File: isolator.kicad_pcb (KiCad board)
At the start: 4 copper layers, 120 x 75 mm, 125 parts, among them J1 HOST, J2 USB_C_Receptacle_PowerOnly_6P, J3 USB_A, J4 USB_A, J5 USB_C_Receptacle_USB2.0_16P, J6 USB_C_Receptacle_USB2.0_16P, Q1 2N7002, Q2 2N7002, T1 750313638, U1 ADuM4165, U10 TPS2553DBV, U11 TPS2553DBV, U12 TPS2553DBV, U13 TLV7041DBV, U14 TLV7041DBV, U15 USBLC6-2SC6, U16 USBLC6-2SC6, U17 USBLC6-2SC6, U18 USBLC6-2SC6, U2 USBLC6-2SC6, U3 USBLC6-2SC6, U4 USB2514B_Bi, U5 SN6505BDBV, U6 MIC29302WU, U7 TPS2121, U8 AP2112K-3.3, U9 TPS2553DBV, Y1 24M 8pF, Y2 24M 12pF

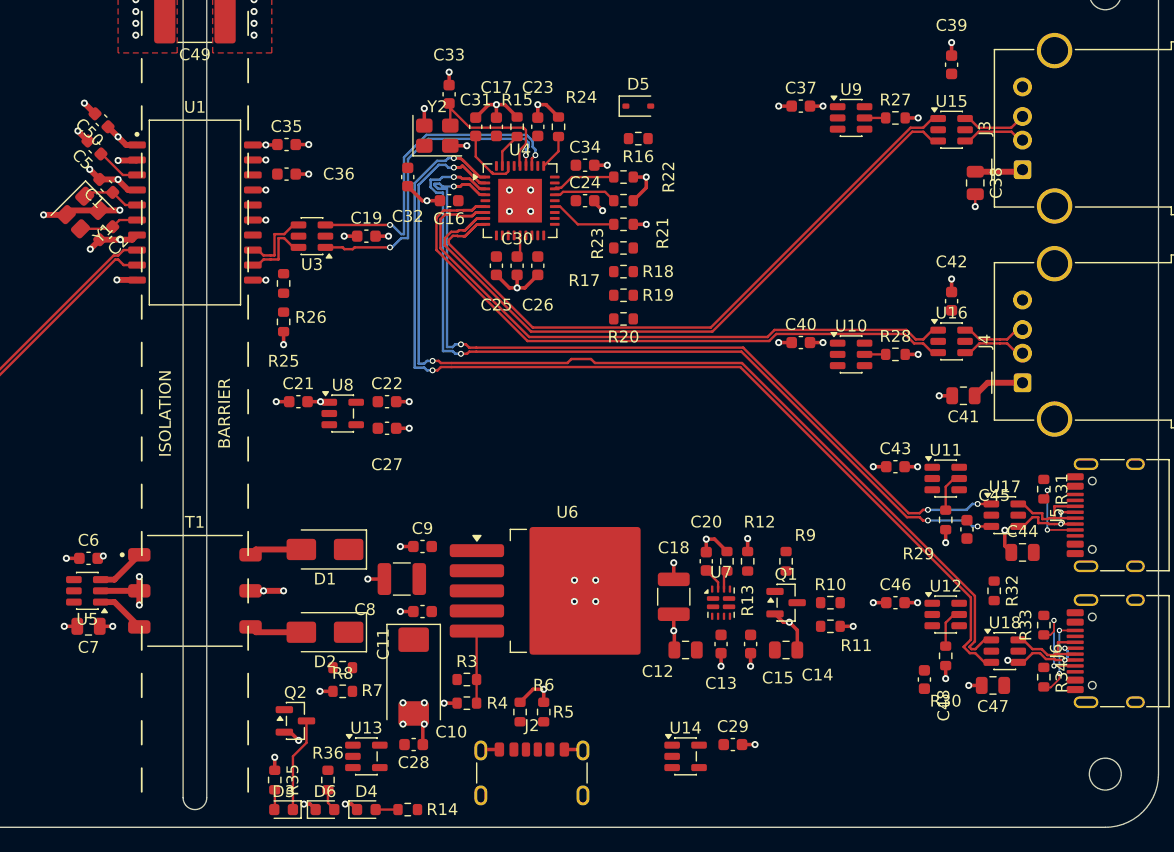
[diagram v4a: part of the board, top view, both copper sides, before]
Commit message: feat(pcb): autoroute remaining nets via Freerouting pipeline — 110 nets landed (146->36 unconnected), pairs verified conserved, planes locked out, PGOOD2 barrier fix
Co-Authored-By: Claude Fable 5 <noreply@anthropic.com>
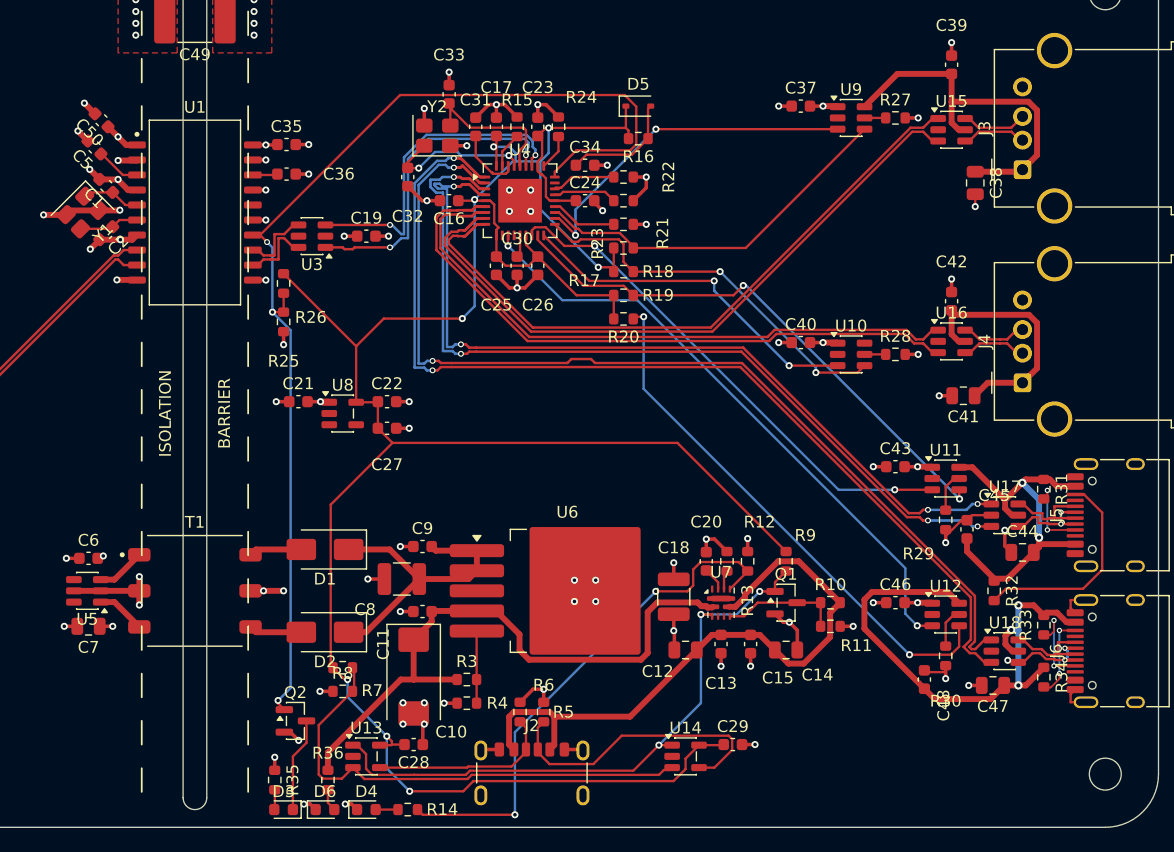
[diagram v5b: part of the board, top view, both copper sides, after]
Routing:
- net /ISO_3V3: track 0.00 -> 215.9 mm, vias 0 -> 8
- net /PGOOD2: track 0.00 -> 93.6 mm, vias 0 -> 3
- net /EXT_5V: track 0.00 -> 54.0 mm
- net /n3A_DET: track 0.00 -> 52.5 mm, vias 0 -> 3
- net /PRTPWR4: track 0.00 -> 52.3 mm, vias 0 -> 2
- net /DCDC_5V: track 0.00 -> 51.9 mm
- net /nOCS3: track 0.00 -> 46.6 mm, vias 0 -> 2
- net /P4_VBUS: track 0.00 -> 45.6 mm, vias 0 -> 3
- net /nOCS4: track 0.00 -> 45.1 mm, vias 0 -> 2
- net /ST_IND: track 0.00 -> 44.3 mm, vias 0 -> 2
- net /PRTPWR3: track 0.00 -> 43.6 mm, vias 0 -> 2
- net /VTH: track 0.00 -> 41.6 mm
- net /nOCS2: track 0.00 -> 32.9 mm, vias 0 -> 2
- net /P3_VBUS: track 0.00 -> 32.5 mm, vias 0 -> 2
- net /nOCS1: track 0.00 -> 31.7 mm
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
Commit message: wip(4port): save in-progress 4-port schematic/PCB edits before archiving
Snapshot of the uncommitted work on the 4-port isolator so it is preserved
before the repo collapses to the single-port design at the root.

State of this snapshot: ERC reports 3 errors, all U7 (TPS2121) pin 4 OV2
disconnected. That is pre-existing, in-progress work on the 4-port design --
it is NOT a regression introduced here and is deliberately left unfixed.

This commit is the tip of branch 4port-archive; main proceeds without the
4-port project.

Co-Authored-By: Claude Opus 5 <noreply@anthropic.com>
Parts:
- moved R25 2.46 mm to (97.4, 82.3)
- moved R26 2.46 mm to (97.4, 79.0)
- moved U3 1.92 mm to (99.1, 74.8)
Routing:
- net /nOCS4: track 45.1 -> 61.5 mm, vias 2 -> 4
- net /ISO_D+: track 33.4 -> 26.7 mm
- net /ISO_D-: track 33.9 -> 27.3 mm
- net /HUB_RESET: track 9.88 -> 12.4 mm
- net /PGOOD2: track 93.6 -> 95.9 mm
- net /ISO_3V3: track 215.9 -> 213.7 mm

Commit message: refactor: collapse repo to the single-port isolator at the root
The single-port design is the one that ships, so it moves up from v1/ and
becomes the only KiCad project in the repo. The 4-port design is archived on
branch 4port-archive (tip ef23a53) and removed from main.

Moved (via git mv, history preserved):
  v1/isolator-v1.kicad_{sch,pcb,pro,dru} -> isolator.kicad_{sch,pcb,pro,dru}
  v1/isolator-v1-bom.csv                 -> isolator-bom.csv
  v1/{sym,fp}-lib-table                  -> {sym,fp}-lib-table
  analysis-v1/                           -> analysis/

Deleted (4-port project and its artifacts): isolator.kicad_{sch,pcb,pro,prl,dru},
isolator-erc.rpt, isolator-backups/, analysis/, logs/. Kept isolator-lib.kicad_sym,
isolator-lib.pretty/, datasheets/, docs/, tools/.

Path and self-reference fixes the move required:
  - {sym,fp}-lib-table URIs: ${KIPRJMOD}/../isolator-lib.* -> ${KIPRJMOD}/isolator-lib.*
  - isolator.kicad_pro: meta.filename and schematic.top_level_sheets[0].filename/name,
    plus sheets[0]. The sheet UUID already matched the schematic root uuid
    (00000000-0000-0000-0000-000000000001) and was left alone. kicad-cli never
    reads these fields, so nothing but a GUI open would have caught them.
  - isolator.kicad_sch: 62 (project "isolator-v1") instance blocks -> "isolator",
    so the GUI keeps its per-project symbol instance data.
  - Schematic text block "V1 LAYOUT CONSTRAINTS -- BINDING" -> "LAYOUT CONSTRAINTS
    -- BINDING"; title block "Isolated USB 2.0 Cable — v1" -> "Isolated USB 2.0
    Cable". Rev "v1.0" left as-is: that is a revision, not a design name.
  - docs/superpowers/{specs,plans,reviews}/*.md: paths updated, "v1" as a design
    name rewritten to "the isolator", "v2" to "the archived 4-port design".
    References to the 4-port files now read 4port-archive:isolator.kicad_sch, since
    that path at the root means the single-port design now. Every doc carries a
    dated banner explaining the restructure; past-tense decisi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
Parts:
- removed C1, C2: 8p, Capacitor_SMD:C_0603_1608Metric
- removed C10: 47u, Capacitor_Tantalum_SMD:CP_EIA-7343-31_Kemet-D
- removed C11, C13, C15, C16, C17, C19, C20, C23, C24, C25, C26, C27, C28, C29, C30, C31, C35, C36, C37, C39, C40, C42, C43, C45, C46, C48, C6, C9: 0.1u, Capacitor_SMD:C_0603_1608Metric
- removed C12, C14, C3, C7: 10u, Capacitor_SMD:C_0805_2012Metric
- removed C18, C8: 47u, Capacitor_SMD:C_1210_3225Metric
- removed C21, C22, C34: 1u, Capacitor_SMD:C_0603_1608Metric
- removed C32, C33: 18p, Capacitor_SMD:C_0603_1608Metric
- removed C38, C41, C44, C47: 22u, Capacitor_SMD:C_0805_2012Metric
- removed C4, C5, C50: 100n, Capacitor_SMD:C_0603_1608Metric
- removed C49: 1nF 2kV DNP, Capacitor_SMD:C_2220_5750Metric
- removed D1, D2: SS34, Diode_SMD:D_SMA
- removed D3, D4, D6: LED, LED_SMD:LED_0603_1608Metric
- removed D5: 1N4148WS, Diode_SMD:D_SOD-323
- removed J1: HOST, Connector_USB:USB_C_Receptacle_HRO_TYPE-C-31-M-12
- removed J2: USB_C_Receptacle_PowerOnly_6P, Connector_USB:USB_C_Receptacle_GCT_USB4125-xx-x_6P_TopMnt_Horizontal
- removed J3, J4: USB_A, Connector_USB:USB_A_Molex_67643_Horizontal
- removed J5, J6: USB_C_Receptacle_USB2.0_16P, Connector_USB:USB_C_Receptacle_HRO_TYPE-C-31-M-12
- removed MH1, MH2, MH3, MH4: MountingHole_2.7mm_M2.5_DIN965, MountingHole:MountingHole_2.7mm_M2.5_DIN965
- removed Q1, Q2: 2N7002, Package_TO_SOT_SMD:SOT-23
- removed R1, R2, R5, R6: 5.1k, Resistor_SMD:R_0603_1608Metric
- removed R10, R17, R18, R19, R20, R25, R26, R9: 100k, Resistor_SMD:R_0603_1608Metric
- removed R11, R23, R24: 47k, Resistor_SMD:R_0603_1608Metric
- removed R12: 35.7k, Resistor_SMD:R_0603_1608Metric
- removed R13, R16, R21, R22, R4, R8: 10k, Resistor_SMD:R_0603_1608Metric
- removed R14, R35: 1k, Resistor_SMD:R_0603_1608Metric
- removed R15: 12.0k, Resistor_SMD:R_0603_1608Metric
- removed R27, R28, R29, R30: 40.2k, Resistor_SMD:R_0603_1608Metric
- removed R3: 30.1k, Resistor_SMD:R_0603_1608Metric
- removed R31, R32, R33, R34: 56k, Resistor_SMD:R_0603_1608Metric
- removed R36: 330R, Resistor_SMD:R_0603_1608Metric
- removed R7: 16.9k, Resistor_SMD:R_0603_1608Metric
- removed T1: 750313638, isolator-lib:WE_750313638
- removed U1: ADuM4165, isolator-lib:ADI_SOIC_IC_20_RI-20-1
- removed U10, U11, U12, U9: TPS2553DBV, Package_TO_SOT_SMD:SOT-23-6
- removed U13, U14: TLV7041DBV, Package_TO_SOT_SMD:SOT-23-5
- removed U15, U16, U17, U18, U2, U3: USBLC6-2SC6, Package_TO_SOT_SMD:SOT-23-6
- removed U4: USB2514B_Bi, Package_DFN_QFN:QFN-36-1EP_6x6mm_P0.5mm_EP3.7x3.7mm
- removed U5: SN6505BDBV, Package_TO_SOT_SMD:SOT-23-6
- removed U6: MIC29302WU, Package_TO_SOT_SMD:TO-263-5_TabPin3
- removed U7: TPS2121, Package_DFN_QFN:Texas_VQFN-HR-12_2x2.5mm_P0.5mm
- removed U8: AP2112K-3.3, Package_TO_SOT_SMD:SOT-23-5
- removed Y1: 24M 8pF, Crystal:Crystal_SMD_3225-4Pin_3.2x2.5mm
- removed Y2: 24M 12pF, Crystal:Crystal_SMD_3225-4Pin_3.2x2.5mm
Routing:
- net /ISO_3V3: track 213.7 -> 0.00 mm, vias 8 -> 0
- net GND2: track 109.1 -> 0.00 mm, vias 71 -> 0
- net /P4_D-: track 96.5 -> 0.00 mm, vias 5 -> 0
- net /PGOOD2: track 95.9 -> 0.00 mm, vias 3 -> 0
- net /P4_D+: track 95.8 -> 0.00 mm, vias 2 -> 0
- net /P3_D-: track 84.0 -> 0.00 mm, vias 6 -> 0
- net /P3_D+: track 83.4 -> 0.00 mm, vias 4 -> 0
- net /P1_D-: track 64.6 -> 0.00 mm
- net /P1_D+: track 63.5 -> 0.00 mm
- net /nOCS4: track 61.5 -> 0.00 mm, vias 4 -> 0
- net /P2_D-: track 61.3 -> 0.00 mm
- net /P2_D+: track 60.2 -> 0.00 mm
- net /EXT_5V: track 54.0 -> 0.00 mm
- net /n3A_DET: track 52.5 -> 0.00 mm, vias 3 -> 0
- net /PRTPWR4: track 52.3 -> 0.00 mm, vias 2 -> 0
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- removed copper zone on In2.Cu, net /ISO_5V
- removed copper zone on In2.Cu, net /VBUS_HOST
- removed copper zone on F.Cu, net GND1
- removed copper zone on In1.Cu, net GND1
- removed copper zone on F.Cu, net GND2
- removed copper zone on In1.Cu, net GND2
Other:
- board outline removed
- board text removed: "BARRIER"
- board text removed: "ISOLATION"

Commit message: feat(pcb): board skeleton -- 120x50 outline, JLC04161H-7628 stackup, edge keepouts, Gate 2
Also corrects the stackup's source branch in the spec and plan. It is on
claude/jlcpcb-design-rules-4layer-6d6ae1 (5c56d3e), not 4port-archive -- the
archived 4-port board still carries the stale 2-layer stackup (1.51mm core,
Er 4.5) that 5c56d3e was written to replace.

The plan's sed-based extraction was also wrong: a sed range on
/(stackup/,/^\t\t)/ closes early on this file and drops In1.Cu and In2.Cu while
still yielding balanced parentheses, so the truncation reads as success. Now
extracted by paren matching.

Co-Authored-By: Claude Opus 5 <noreply@anthropic.com>
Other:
- board outline added: 120 x 50 mm
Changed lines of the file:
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@@
 	(layers
 		(0 "F.Cu" signal)
-		(4 "In1.Cu" signal "GND")
-		(6 "In2.Cu" signal "PWR")
+		(4 "In1.Cu" signal "GND_SPLIT_A")
+		(6 "In2.Cu" signal "GND_SPLIT_B")
 		(2 "B.Cu" signal)
 		(9 "F.Adhes" user "F.Adhesive")
@@
 		(33 "B.Fab" user)
 	)
+	(setup
+		(stackup
+			(layer "F.SilkS"
+				(type "Top Silk Screen")
+			)
+			(layer "F.Paste"
+				(type "Top Solder Paste")
+			)
+			(layer "F.Mask"
+				(type "Top Solder Mask")
+				(color "Green")
+				(thickness 0.01)
+			)
+			(layer "F.Cu"
+				(type "copper")
+				(thickness 0.035)
+			)
+			(layer "dielectric 1"
+				(type "prepreg")
+				(thickness 0.2104)
+				(material "FR4")
+				(epsilon_r 4.4)
+				(loss_tangent 0.02)
+			)
+			(layer "In1.Cu"
+				(type "copper")
+				(thickness 0.0152)
+			)
+			(layer "dielectric 2"
+				(type "core")
+				(thickness 1.065)
+				(material "FR4")
+				(epsilon_r 4.6)
+				(loss_tangent 0.02)
+			)
+			(layer "In2.Cu"
+				(type "copper")
+				(thickness 0.0152)
+			)
+			(layer "dielectric 3"
+				(type "prepreg")
+				(thickness 0.2104)
+				(material "FR4")
+				(epsilon_r 4.4)
+				(loss_tangent 0.02)
+			)
+			(layer "B.Cu"
+				(type "copper")
+				(thickness 0.035)
+			)
+			(layer "B.Mask"
+				(type "Bottom Solder Mask")
+				(color "Green")
+				(thickness 0.01)
+			)
+			(layer "B.Paste"
+				(type "Bottom Solder Paste")
+			)
+			(layer "B.SilkS"
+				(type "Bottom Silk Screen")
+			)
+			(copper_finish "None")
+			(dielectric_constraints no)
+		)
+		(pad_to_mask_clearance 0)
+		(allow_soldermask_bridges_in_footprints no)
+		(tenting
+			(front yes)
+			(back yes)
+		)
+		(covering
+			(front no)
+			(back no)
+		)
+		(plugging
+			(front no)
+			(back no)
+		)
+		(capping no)
+		(filling no)
+		(pcbplotparams
+			(layerselection 0x00000000_00000000_55555555_5755f5ff)
+			(plot_on_all_layers_selection 0x00000000_00000000_00000000_00000000)
+			(disableapertmacros no)
+			(usegerberextensions no)
+			(usegerberattributes yes)
+			(usegerberadvancedattributes yes)
+			(creategerberjobfile yes)
+			(dashed_line_dash_ratio 12)
+			(dashed_line_gap_ratio 3)
+			(svgprecision 4)
+			(plotframeref no)
+			(mode 1)
+			(useauxorigin no)
+			(pdf_front_fp_property_popups yes)
+			(pdf_back_fp_property_popups yes)
+			(pdf_metadata yes)
+			(pdf_single_document no)
+			(dxfpolygonmode yes)
+			(dxfimperialunits yes)
+			(dxfusepcbnewfont yes)
+			(psnegative no)
+			(psa4output no)
+			(plot_black_and_white yes)
+			(sketchpadsonfab no)
+			(plotpadnumbers no)
+			(hidednponfab no)
+			(sketchdnponfab yes)
+			(crossoutdnponfab yes)
+			(subtractmaskfromsilk no)
+			(outputformat 1)
+			(mirror no)
+			(drillshape 1)
+			(scaleselection 1)
+			(outputdirectory "")
+		)
+	)
+	(gr_line
+		(start 0 0)
+		(end 120 0)
+		(stroke
+			(width 0.1)
+			(type default)
+		)
+		(layer "Edge.Cuts")
+	)
+	(gr_line
+		(start 0 50)
+		(end 0 0)
+		(stroke
+			(width 0.1)
+			(type default)
+		)
+		(layer "Edge.Cuts")
+	)
+	(gr_line
+		(start 120 0)
+		(end 120 50)
+		(stroke
+			(width 0.1)
+			(type default)
+		)
+		(layer "Edge.Cuts")
+	)
+	(gr_line
+		(start 120 50)
+		(end 0 50)
+		(stroke
+			(width 0.1)
+			(type default)
+		)
+		(layer "Edge.Cuts")
+	)
+	(zone
+		(layers "F.Cu" "B.Cu" "In1.Cu" "In2.Cu")
+		(hatch edge 0.5)
+		(connect_pads thru_hole_only
+			(clearance 0)
+		)
+		(min_thickness 0.25)
+		(keepout
+			(tracks not_allowed)
+			(vias not_allowed)
+			(pads not_allowed)
+			(copperpour not_allowed)
+			(footprints allowed)
+		)
+		(placement
+			(enabled no)
+			(sheetname "")
+		)
+		(fill
+			(thermal_gap 0.5)
+			(thermal_bridge_width 0.5)
+			(smoothing chamfer)
+			(radius 0.5)
+			(island_removal_mode 0)
+		)
+		(polygon
+			(pts
+				(xy 0 0) (xy 120 0) (xy 120 2) (xy 0 2)
+			)
+		)
+	)
+	(zone
+		(layers "F.Cu" "B.Cu" "In1.Cu" "In2.Cu")
+		(hatch edge 0.5)
+		(connect_pads thru_hole_only
+			(clearance 0)
+		)
+		(min_thickness 0.25)
+		(keepout
+			(tracks not_allowed)
+			(vias not_allowed)
+			(pads not_allowed)
+			(copperpour not_allowed)
+			(footprints allowed)
+		)
+		(placement
+			(enabled no)
+			(sheetname "")
+		)
+		(fill
+			(thermal_gap 0.5)
+			(thermal_bridge_width 0.5)
+			(smoothing chamfer)
+			(radius 0.5)
+			(island_removal_mode 0)
+		)
+		(polygon
+			(pts
+				(xy 0 48) (xy 120 48) (xy 120 50) (xy 0 50)
+			)
+		)
+	)
+	(embedded_fonts no)
 )
